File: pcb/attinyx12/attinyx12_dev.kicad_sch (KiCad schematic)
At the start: 24 parts, among them J1 USB_C_Receptacle_USB2.0_16P, J2 Conn_01x04, J3 Conn_01x04, J4 Conn_02x06, U1 USBLC6-2SC6, U2 ATtiny212-SS, U3 CH342K

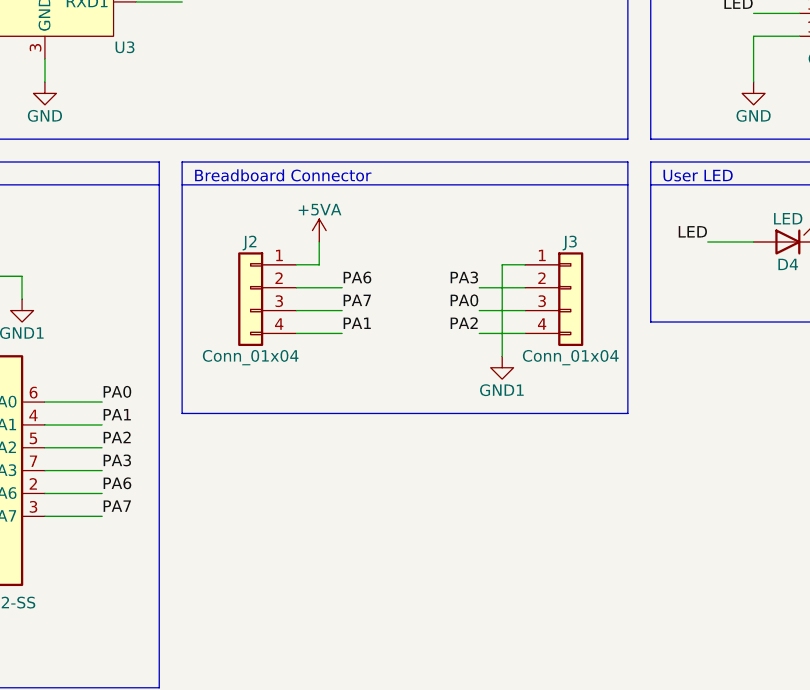
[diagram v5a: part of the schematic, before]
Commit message: add silkscreen
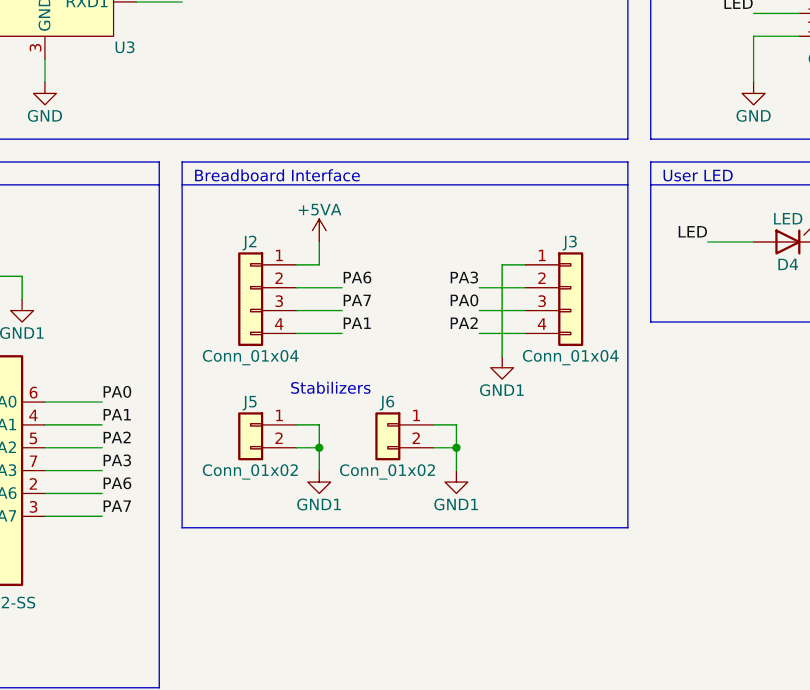
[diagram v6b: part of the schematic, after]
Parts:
- added J5, J6: Conn_01x02, Connector_PinHeader_2.54mm:PinHeader_1x02_P2.54mm_Vertical, symbol Connector_Generic:Conn_01x02
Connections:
- net GND1: now also J5.1 (Pin_1), J5.2 (Pin_2), J6.1 (Pin_1), J6.2 (Pin_2)
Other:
- note added: "Breadboard Interface"
- note added: "Stabilizers"
- note removed: "Breadboard Connector"

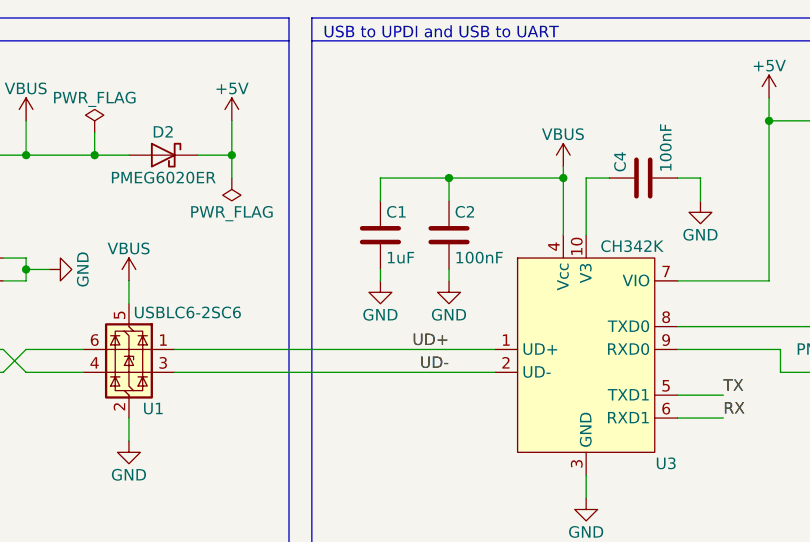
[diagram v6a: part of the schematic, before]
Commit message: update components with MPN, SPN, etc
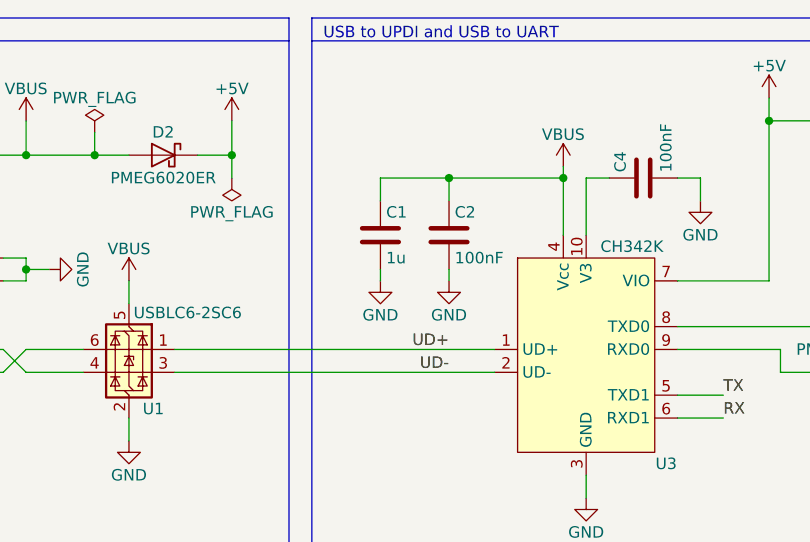
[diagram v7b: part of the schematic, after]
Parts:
- C1: value 1uF -> 1u; MPN (none) -> FS18F105Z160PBG; Manufacture (none) -> PSA(Prosperity Dielectrics); SPN (none) -> C363560; Supplier (none) -> LCSC; Voltage (none) -> 16V
- C2, C4: MPN (none) -> CL10B104KO8NNNC; Manufacture (none) -> Samsung Electro-Mechanics; SPN (none) -> C66501; Supplier (none) -> LCSC; Voltage (none) -> 16V
- C3, C5: MPN (none) -> FS18F105Z160PBG; Manufacture (none) -> PSA(Prosperity Dielectrics); SPN (none) -> C363560; Supplier (none) -> LCSC; Voltage (none) -> 16V
- D1, D4: MPN (none) -> NCD0603R1; Manufacture (none) -> Foshan NationStar Optoelectronics; Power (none) -> 25mA; SPN (none) -> C84263; Supplier (none) -> LCSC; Voltage (none) -> 1.6V-2.6V
- D2, D3: MPN (none) -> PMEG6020ER,115; Manufacture (none) -> Nexperia; Power (none) -> 2A; SPN (none) -> C98663; Supplier (none) -> LCSC; Voltage (none) -> 60V
- F1: MPN (none) -> MF-PSMF075X-2; Manufacture (none) -> BOURNS; Power (none) -> 750mA; SPN (none) -> C116173; Supplier (none) -> LCSC; Voltage (none) -> 6V
- J1: MPN (none) -> GT-USB-7010ASV; Manufacture (none) -> G-Switch; Power (none) -> 3A; SPN (none) -> C2988369; Supplier (none) -> LCSC; Voltage (none) -> 24V
- J2, J3: MPN (none) -> IPCP254M04PB08V; Manufacture (none) -> INCP; Power (none) -> 3A; SPN (none) -> C22438419; Supplier (none) -> LCSC
- J4: MPN (none) -> IPCP254M12PB28V; Manufacture (none) -> INCP; Power (none) -> 3A; SPN (none) -> C22438442; Supplier (none) -> LCSC
- J5, J6: MPN (none) -> IPCP254M02PB08V; Manufacture (none) -> INCP; Power (none) -> 3A; SPN (none) -> C22395601; Supplier (none) -> LCSC
- R1, R4: MPN (none) -> RC1608J102CS; Manufacture (none) -> Samsung Electro-Mechanics; Power (none) -> 100mW; SPN (none) -> 1276-5062-1-ND; Supplier (none) -> DigiKey; Tolerance (none) -> 5%
- R2, R3: MPN (none) -> RC0603FR-075K1L; Manufacture (none) -> YAGEO; Power (none) -> 100mW; SPN (none) -> C105580; Supplier (none) -> LCSC; Tolerance (none) -> 1%
- R5: MPN (none) -> RC0805FR-07470RL; Manufacture (none) -> YAGEO; Power (none) -> 125mW; SPN (none) -> 311-470CRCT-ND; Supplier (none) -> DigiKey; Tolerance (none) -> 1%
- U1: MPN (none) -> USBLC6-2SC6; Manufacture (none) -> STMicroelectronics; Power (none) -> 5A; SPN (none) -> C7519; Supplier (none) -> LCSC; Voltage (none) -> 17V 6V
- U2: MPN (none) -> ATTINY212-SSN; Manufacture (none) -> Microchip Technology; SPN (none) -> ATTINY212-SSN-ND; Supplier (none) -> DigiKey
- U3: MPN (none) -> CH342K; Manufacture (none) -> WCH; SPN (none) -> C2826608; Supplier (none) -> LCSC
